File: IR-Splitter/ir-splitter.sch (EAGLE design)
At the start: 33 parts, among them T1 IRFR024N, T10 IRFR024N, T2 IRFR024N, T3 IRFR024N, T4 IRFR024N, T5 IRFR024N, T6 IRFR024N, T7 IRFR024N, T8 IRFR024N, T9 IRFR024N, X1 250-202

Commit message: Updated IR-Splitter
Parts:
- removed JP1, JP2: (no value), pinhead:PINHD-1X4/90
- removed LED1: (no value), led:LED5MM
- removed R2: 300R, rcl:R-EU_0207/15
- removed SUPPLY_OUT: (no value), wirepad:3,81/1,4
- renumbered PAD1 to IR_DATA, PAD3 to GND, X1 to SUPPLY
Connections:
- removed net N$1: LED1.A, R2.1
- net +12V: no longer JP1.2, JP1.3, JP2.2, JP2.3, R2.2, SUPPLY_OUT.P
- net GND: no longer JP1.1, JP1.4, JP2.1, JP2.4
- net IR-IN-DATA: no longer LED1.C
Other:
- note added: "v0.0.1"
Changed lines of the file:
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@@
 <?xml version="1.0" encoding="utf-8"?>
 <!DOCTYPE eagle SYSTEM "eagle.dtd">
-<eagle version="6.1">
+<eagle version="6.3">
 <drawing>
 <settings>
@@
 <parts>
 <part name="FRAME1" library="frames" deviceset="A4L-LOC" device=""/>
-<part name="X1" library="con-wago_250" deviceset="250-202" device=""/>
+<part name="SUPPLY" library="con-wago_250" deviceset="250-202" device=""/>
 <part name="P+1" library="supply1" deviceset="+12V" device=""/>
 <part name="GND1" library="supply1" deviceset="GND" device=""/>
-<part name="JP1" library="pinhead" deviceset="PINHD-1X4" device="/90"/>
-<part name="JP2" library="pinhead" deviceset="PINHD-1X4" device="/90"/>
-<part name="P+2" library="supply1" deviceset="+12V" device=""/>
-<part name="GND2" library="supply1" deviceset="GND" device=""/>
 <part name="T1" library="international" deviceset="IRLR3915PBF" device="" value="IRFR024N"/>
-<part name="PAD1" library="wirepad" deviceset="3,81/1,4" device="" value="IR-IN-DATA"/>
+<part name="IR_DATA" library="wirepad" deviceset="3,81/1,4" device="" value="IR-IN-DATA"/>
 <part name="IR-OUT1" library="wirepad" deviceset="3,81/1,4" device=""/>
 <part name="GND3" library="supply1" deviceset="GND" device=""/>
-<part name="PAD3" library="wirepad" deviceset="3,81/1,4" device="" value="IR-IN-GND"/>
+<part name="GND" library="wirepad" deviceset="3,81/1,4" device="" value="IR-IN-GND"/>
 <part name="GND4" library="supply1" deviceset="GND" device=""/>
 <part name="P+3" library="supply1" deviceset="+12V" device=""/>
 <part name="R1" library="rcl" deviceset="R-EU_" device="0207/15" value="1k"/>
-<part name="R2" library="rcl" deviceset="R-EU_" device="0207/15" value="300R"/>
-<part name="P+4" library="supply1" deviceset="+12V" device=""/>
-<part name="LED1" library="led" deviceset="LED" device="5MM"/>
 <part name="T2" library="international" deviceset="IRLR3915PBF" device="" value="IRFR024N"/>
 <part name="IR-OUT2" library="wirepad" deviceset="3,81/1,4" device=""/>
@@
 <part name="GND14" library="supply1" deviceset="GND" device=""/>
 <part name="GND15" library="supply1" deviceset="GND" device=""/>
-<part name="SUPPLY_OUT" library="wirepad" deviceset="3,81/1,4" device=""/>
 </parts>
 <sheets>
@@
 <text x="162.56" y="12.7" size="1.9304" layer="94">24149 Kiel</text>
 <text x="162.56" y="7.62" size="1.9304" layer="94">www.northern-stars.de</text>
+<text x="215.9" y="20.32" size="2.54" layer="94">v0.0.1</text>
 </plain>
 <instances>
 <instance part="FRAME1" gate="G$1" x="0" y="0"/>
-<instance part="X1" gate="G$1" x="15.24" y="149.86" rot="R180"/>
+<instance part="SUPPLY" gate="G$1" x="15.24" y="149.86" rot="R180"/>
 <instance part="P+1" gate="1" x="25.4" y="170.18"/>
 <instance part="GND1" gate="1" x="25.4" y="134.62"/>
-<instance part="JP1" gate="A" x="12.7" y="111.76" rot="R180"/>
-<instance part="JP2" gate="A" x="12.7" y="91.44" rot="R180"/>
-<instance part="P+2" gate="1" x="25.4" y="124.46"/>
-<instance part="GND2" gate="1" x="22.86" y="76.2"/>
 <instance part="T1" gate="G$1" x="68.58" y="149.86"/>
-<instance part="PAD1" gate="1" x="12.7" y="35.56"/>
+<instance part="IR_DATA" gate="1" x="12.7" y="35.56"/>
 <instance part="IR-OUT1" gate="1" x="73.66" y="167.64" rot="R270"/>
 <instance part="GND3" gate="1" x="73.66" y="132.08"/>
-<instance part="PAD3" gate="1" x="12.7" y="25.4"/>
+<instance part="GND" gate="1" x="12.7" y="25.4"/>
 <instance part="GND4" gate="1" x="25.4" y="15.24"/>
 <instance part="P+3" gate="1" x="22.86" y="63.5"/>
 <instance part="R1" gate="G$1" x="22.86" y="53.34" rot="R90"/>
-<instance part="R2" gate="G$1" x="38.1" y="53.34" rot="R90"/>
-<instance part="P+4" gate="1" x="38.1" y="63.5"/>
-<instance part="LED1" gate="G$1" x="38.1" y="43.18"/>
 <instance part="T2" gate="G$1" x="114.3" y="149.86"/>
 <instance part="IR-OUT2" gate="1" x="119.38" y="167.64" rot="R270"/>
@@
 <instance part="GND14" gate="1" x="53.34" y="7.62"/>
 <instance part="GND15" gate="1" x="111.76" y="7.62"/>
-<instance part="SUPPLY_OUT" gate="1" x="33.02" y="170.18" rot="R270"/>
 </instances>
 <busses>
@@
 <net name="+12V" class="0">
 <segment>
-<pinref part="X1" gate="G$1" pin="P2"/>
+<pinref part="SUPPLY" gate="G$1" pin="P2"/>
 <pinref part="P+1" gate="1" pin="+12V"/>
 <wire x1="17.78" y1="152.4" x2="25.4" y2="152.4" width="0.1524" layer="91"/>
-<wire x1="25.4" y1="152.4" x2="25.4" y2="162.56" width="0.1524" layer="91"/>
-<pinref part="SUPPLY_OUT" gate="1" pin="P"/>
-<wire x1="25.4" y1="162.56" x2="25.4" y2="167.64" width="0.1524" layer="91"/>
-<wire x1="25.4" y1="162.56" x2="33.02" y2="162.56" width="0.1524" layer="91"/>
-<wire x1="33.02" y1="162.56" x2="33.02" y2="167.64" width="0.1524" layer="91"/>
-<junction x="25.4" y="162.56"/>
-</segment>
-<segment>
-<pinref part="JP1" gate="A" pin="3"/>
-<pinref part="P+2" gate="1" pin="+12V"/>
-<wire x1="15.24" y1="111.76" x2="25.4" y2="111.76" width="0.1524" layer="91"/>
-<wire x1="25.4" y1="111.76" x2="25.4" y2="121.92" width="0.1524" layer="91"/>
-<pinref part="JP1" gate="A" pin="2"/>
-<wire x1="15.24" y1="109.22" x2="25.4" y2="109.22" width="0.1524" layer="91"/>
-<wire x1="25.4" y1="109.22" x2="25.4" y2="111.76" width="0.1524" layer="91"/>
-<junction x="25.4" y="111.76"/>
-<pinref part="JP2" gate="A" pin="3"/>
-<wire x1="15.24" y1="91.44" x2="25.4" y2="91.44" width="0.1524" layer="91"/>
-<wire x1="25.4" y1="91.44" x2="25.4" y2="109.22" width="0.1524" layer="91"/>
-<junction x="25.4" y="109.22"/>
-<pinref part="JP2" gate="A" pin="2"/>
-<wire x1="15.24" y1="88.9" x2="25.4" y2="88.9" width="0.1524" layer="91"/>
-<wire x1="25.4" y1="88.9" x2="25.4" y2="91.44" width="0.1524" layer="91"/>
-<junction x="25.4" y="91.44"/>
+<wire x1="25.4" y1="152.4" x2="25.4" y2="167.64" width="0.1524" layer="91"/>
 </segment>
 <segment>
@@
 <wire x1="22.86" y1="58.42" x2="22.86" y2="60.96" width="0.1524" layer="91"/>
 </segment>
-<segment>
-<pinref part="R2" gate="G$1" pin="2"/>
-<pinref part="P+4" gate="1" pin="+12V"/>
-<wire x1="38.1" y1="60.96" x2="38.1" y2="58.42" width="0.1524" layer="91"/>
-</segment>
 </net>
 <net name="GND" class="0">
 <segment>
-<pinref part="X1" gate="G$1" pin="P1"/>
+<pinref part="SUPPLY" gate="G$1" pin="P1"/>
 <pinref part="GND1" gate="1" pin="GND"/>
 <wire x1="17.78" y1="147.32" x2="25.4" y2="147.32" width="0.1524" layer="91"/>
@@
 </segment>
 <segment>
-<pinref part="JP1" gate="A" pin="4"/>
-<pinref part="GND2" gate="1" pin="GND"/>
-<wire x1="15.24" y1="114.3" x2="22.86" y2="114.3" width="0.1524" layer="91"/>
-<wire x1="22.86" y1="114.3" x2="22.86" y2="106.68" width="0.1524" layer="91"/>
-<pinref part="JP1" gate="A" pin="1"/>
-<wire x1="22.86" y1="106.68" x2="22.86" y2="93.98" width="0.1524" layer="91"/>
-<wire x1="22.86" y1="93.98" x2="22.86" y2="86.36" width="0.1524" layer="91"/>
-<wire x1="22.86" y1="86.36" x2="22.86" y2="78.74" width="0.1524" layer="91"/>
-<wire x1="15.24" y1="106.68" x2="22.86" y2="106.68" width="0.1524" layer="91"/>
-<junction x="22.86" y="106.68"/>
-<pinref part="JP2" gate="A" pin="4"/>
-<wire x1="15.24" y1="93.98" x2="22.86" y2="93.98" width="0.1524" layer="91"/>
-<junction x="22.86" y="93.98"/>
-<pinref part="JP2" gate="A" pin="1"/>
-<wire x1="15.24" y1="86.36" x2="22.86" y2="86.36" width="0.1524" layer="91"/>
-<junction x="22.86" y="86.36"/>
-</segment>
-<segment>
 <pinref part="T1" gate="G$1" pin="P$3"/>
 <pinref part="GND3" gate="1" pin="GND"/>
@@
 </segment>
 <segment>
-<pinref part="PAD3" gate="1" pin="P"/>
+<pinref part="GND" gate="1" pin="P"/>
 <pinref part="GND4" gate="1" pin="GND"/>
 <wire x1="15.24" y1="25.4" x2="25.4" y2="25.4" width="0.1524" layer="91"/>
@@
 <net name="IR-IN-DATA" class="0">
 <segment>
-<pinref part="PAD1" gate="1" pin="P"/>
+<pinref part="IR_DATA" gate="1" pin="P"/>
 <wire x1="15.24" y1="35.56" x2="22.86" y2="35.56" width="0.1524" layer="91"/>
-<label x="43.18" y="35.56" size="1.27" layer="95" xref="yes"/>
+<label x="33.02" y="35.56" size="1.27" layer="95" xref="yes"/>
 <pinref part="R1" gate="G$1" pin="1"/>
-<wire x1="22.86" y1="35.56" x2="38.1" y2="35.56" width="0.1524" layer="91"/>
-<wire x1="38.1" y1="35.56" x2="43.18" y2="35.56" width="0.1524" layer="91"/>
+<wire x1="22.86" y1="35.56" x2="33.02" y2="35.56" width="0.1524" layer="91"/>
 <wire x1="22.86" y1="48.26" x2="22.86" y2="35.56" width="0.1524" layer="91"/>
 <junction x="22.86" y="35.56"/>
-<pinref part="LED1" gate="G$1" pin="C"/>
-<wire x1="38.1" y1="35.56" x2="38.1" y2="38.1" width="0.1524" layer="91"/>
-<junction x="38.1" y="35.56"/>
 </segment>
 <segment>
@@
 </segment>
 </net>
-<net name="N$1" class="0">
-<segment>
-<pinref part="LED1" gate="G$1" pin="A"/>
-<pinref part="R2" gate="G$1" pin="1"/>
-<wire x1="38.1" y1="48.26" x2="38.1" y2="45.72" width="0.1524" layer="91"/>
-</segment>
-</net>

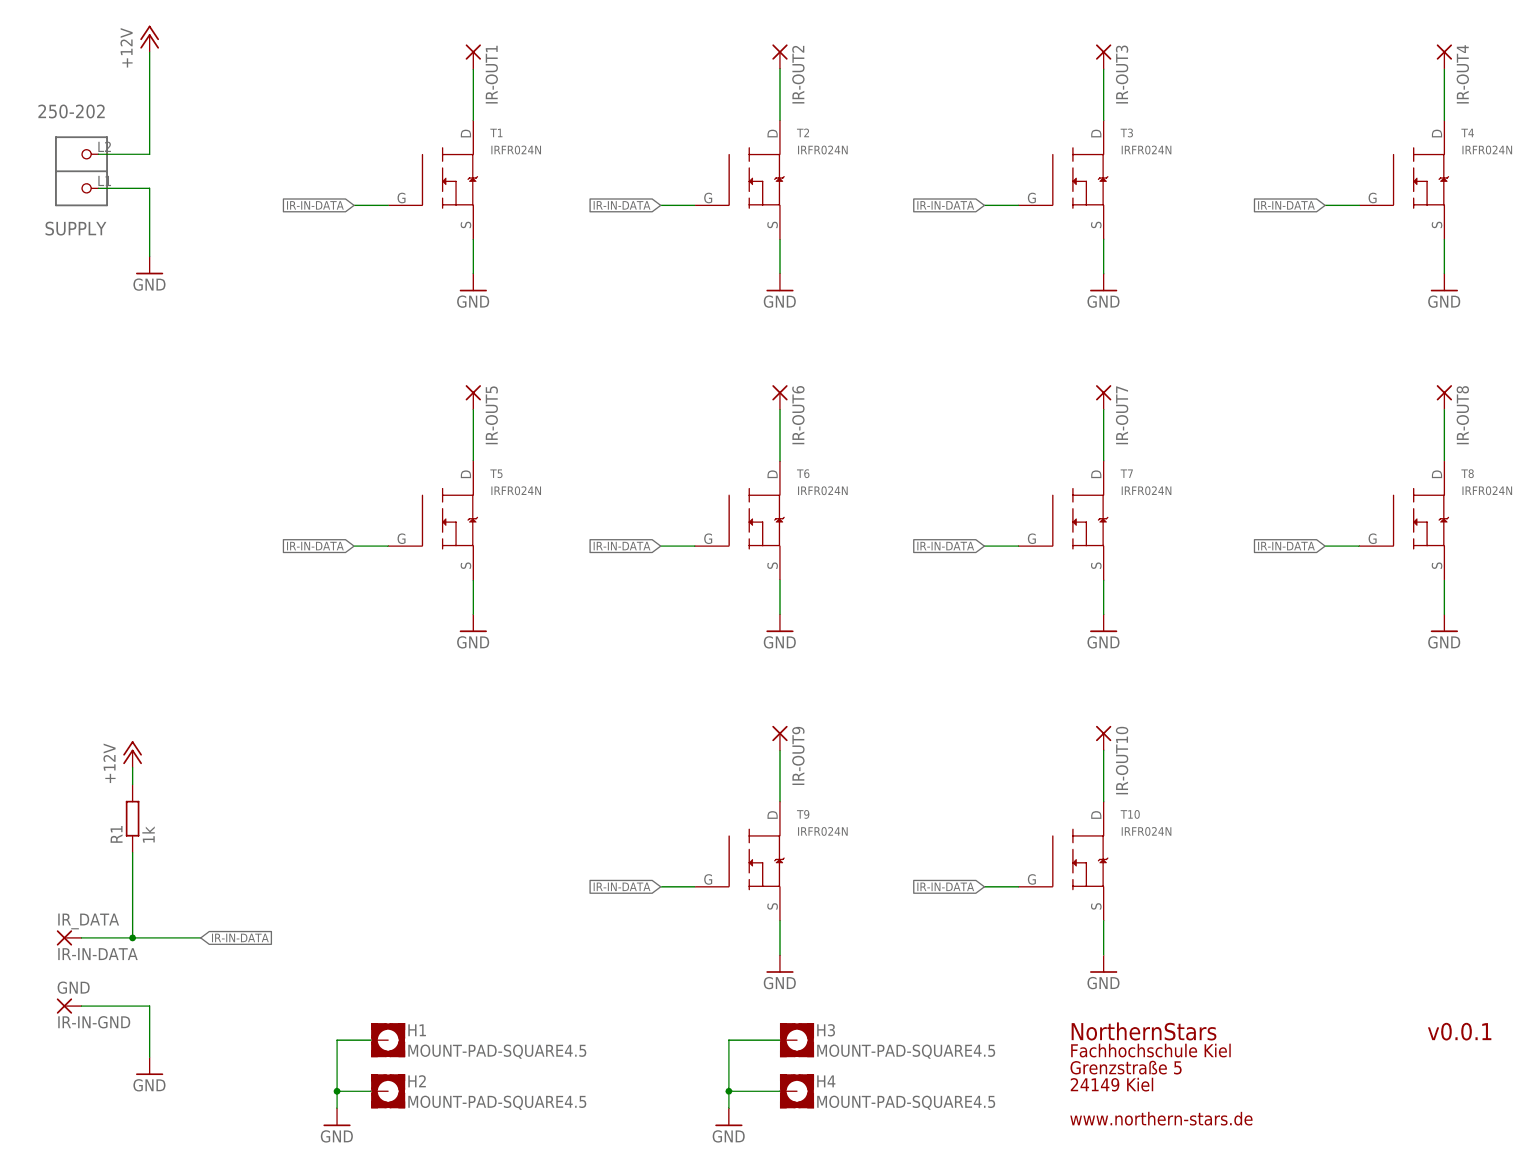
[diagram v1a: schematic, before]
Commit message: Updated IR Splitter schematics and layout to avoid damage of IR leds
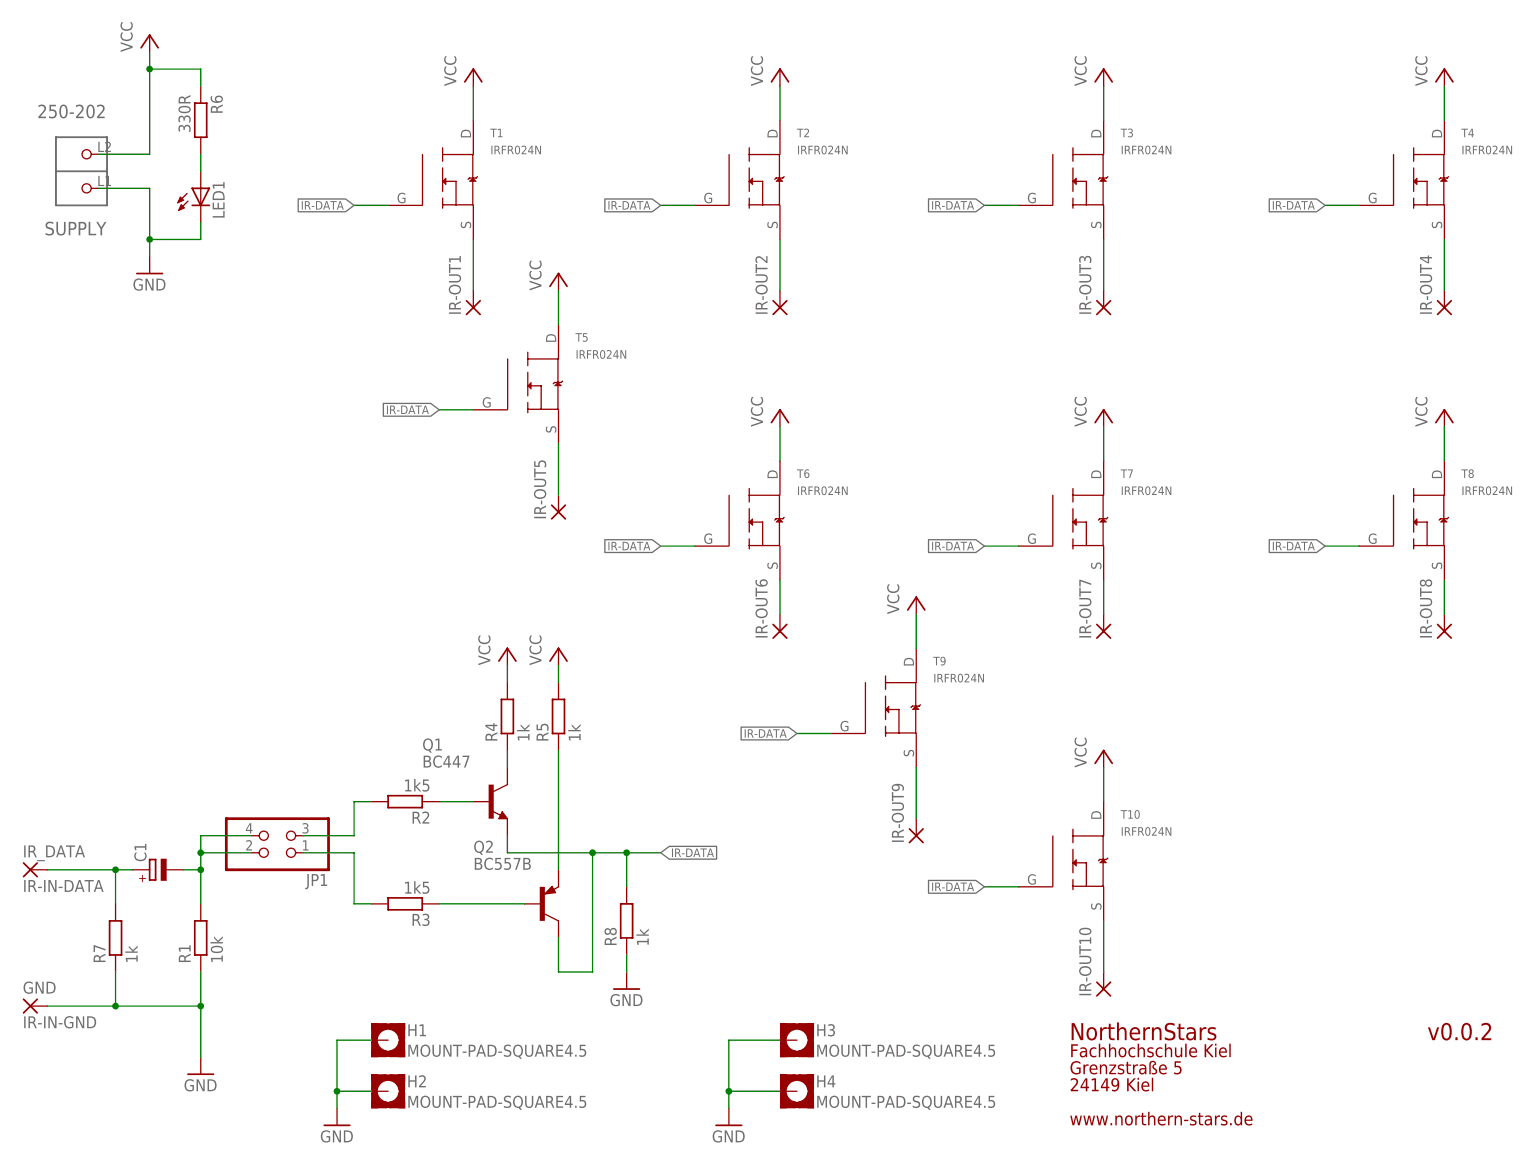
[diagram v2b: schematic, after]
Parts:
- added C1: (no value), rcl:CPOL-EUE2.5-5
- added JP1: (no value), pinhead-2:PINHD-2X02_2.54-SMD
- added LED1: (no value), led:LED3MM
- added Q1: BC447, transistor-npn:BC447
- added Q2: BC557B, transistor-pnp:BC557B
- added R2, R3: 1k5, rcl:R-EU_0207/10
- added R4, R5, R7, R8: 1k, rcl:R-EU_0207/10
- added R6: 330R, rcl:R-EU_0207/10
- R1: value 1k -> 10k; device rcl:R-EU_0207/15 -> rcl:R-EU_0207/10
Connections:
- removed net +12V: R1.2, SUPPLY.P2
- removed net IR-IN-DATA: IR_DATA.P, R1.1, T1.G, T10.G, T2.G, T3.G, T4.G, T5.G, T6.G, T7.G, T8.G, T9.G
- new net DATA: C1.-, JP1.2, JP1.4, R1.2
- new net IR-DATA: Q1.E, Q2.C, R8.2, T1.G, T10.G, T2.G, T3.G, T4.G, T5.G, T6.G, T7.G, T8.G, T9.G
- new net N$1: IR-OUT1.P, T1.P$3
- new net N$12: Q1.C, R4.1
- new net N$13: Q2.E, R5.1
- new net N$14: Q2.B, R3.1
- new net N$15: LED1.A, R6.2
- new net N$16: C1.+, IR_DATA.P, R7.2
- new net N$17: JP1.3, R2.2
- new net N$18: JP1.1, R3.2
- new net VCC: R4.2, R5.2, R6.1, SUPPLY.P2, T1.P$2, T10.P$2, T2.P$2, T3.P$2, T4.P$2, T5.P$2, T6.P$2, T7.P$2, T8.P$2, T9.P$2
- net GND: now also LED1.C, R1.1, R7.1, R8.1; no longer T1.P$3, T10.P$3, T2.P$3, T3.P$3, T4.P$3, T5.P$3, T6.P$3, T7.P$3, T8.P$3, T9.P$3
- net N$10: now also T9.P$3; no longer T9.P$2
- net N$11: now also Q1.B, R2.1; no longer IR-OUT10.P, T10.P$2
- net N$2: now also IR-OUT2.P, T2.P$3; no longer IR-OUT1.P, T1.P$2
- net N$3: now also IR-OUT5.P, T5.P$3; no longer IR-OUT2.P, T2.P$2
- net N$4: now also IR-OUT6.P, T6.P$3; no longer IR-OUT3.P, T3.P$2
- net N$5: now also IR-OUT8.P, T8.P$3; no longer IR-OUT4.P, T4.P$2
- net N$6: now also IR-OUT7.P, T7.P$3; no longer IR-OUT5.P, T5.P$2
- net N$7: now also IR-OUT4.P, T4.P$3; no longer IR-OUT6.P, T6.P$2
- net N$8: now also IR-OUT3.P, T3.P$3; no longer IR-OUT7.P, T7.P$2
- net N$9: now also IR-OUT10.P, T10.P$3; no longer IR-OUT8.P, T8.P$2
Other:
- note added: "v0.0.2"
- note removed: "v0.0.1"
- moved on the sheet: GND, IR-OUT1, IR-OUT10, IR-OUT2, IR-OUT3, IR-OUT4, IR-OUT5, IR-OUT6, IR-OUT7, IR-OUT8, IR-OUT9, IR_DATA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

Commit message: Updated IR-Splitter to Version 1.0.0
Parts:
- removed C1: (no value), rcl:CPOL-EUE2.5-5
- removed JP1: (no value), pinhead-2:PINHD-2X02_2.54-SMD
- added R10, R11, R12, R13, R14, R9: >100k, rcl:R-EU_R1206
- LED1: device led:LED3MM -> led:LEDCHIPLED_1206
- Q1: value BC447 -> BC548B; device transistor-npn:BC447 -> transistor-npn:BC548B
- Q2: value BC557B -> BC548B; device transistor-pnp:BC557B -> transistor-npn:BC548B
- R1: value 10k -> 1k; device rcl:R-EU_0207/10 -> rcl:R-EU_R1206
- R2, R3: value 1k5 -> 1k; device rcl:R-EU_0207/10 -> rcl:R-EU_R1206
- R4, R5, R7, R8: value 1k -> >100k; device rcl:R-EU_0207/10 -> rcl:R-EU_R1206
- R6: device rcl:R-EU_0207/10 -> rcl:R-EU_R1206
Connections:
- removed net DATA: C1.-, JP1.2, JP1.4, R1.2
- removed net N$12: Q1.C, R4.1
- removed net N$13: Q2.E, R5.1
- removed net N$14: Q2.B, R3.1
- removed net N$17: JP1.3, R2.2
- removed net N$18: JP1.1, R3.2
- net GND: now also Q1.E, R10.1, R11.1, R12.1, R13.1, R14.1, R3.1, R4.1, R5.1, R9.1; no longer R1.1
- net IR-DATA: now also Q2.E, R3.2; no longer Q1.E, Q2.C, R8.2
- net N$1: now also R4.2
- net N$10: now also R12.2
- net N$11: now also Q1.C, Q2.B, R1.1; no longer Q1.B, R2.1
- net N$16: now also Q1.B, R2.1; no longer C1.+, R7.2
- net N$2: now also R5.2
- net N$3: now also R14.2
- net N$4: now also R11.2
- net N$5: now also R9.2
- net N$6: now also R10.2
- net N$7: now also R8.2
- net N$8: now also R7.2
- net N$9: now also R13.2
- net VCC: now also Q2.C, R1.2, R2.2; no longer R4.2, R5.2
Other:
- note added: "v1.0.0"
- note removed: "v0.0.2"
- moved on the sheet: IR-OUT10, IR-OUT5, IR-OUT6, IR-OUT7, IR-OUT8, IR-OUT9, Q1, R1, R2, R3, R4, R5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
